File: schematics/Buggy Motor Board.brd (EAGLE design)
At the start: 100 x 80 mm, 42 parts, among them CON0 M025MM, CON1 M025MM, X1 MICROSD, X2 5566-24, X3 5566-24

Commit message: Tweak for Master
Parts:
- moved IC1 51.9 mm to (36.8, 25.4)
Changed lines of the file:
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@@
 <element name="U$10" library="Teensy_3_Series_Board_v1.0" package="TEENSY_3.1+4" value="TEENSY_3.1+4" x="36.83" y="60.96"/>
 <element name="U$1" library="Wetmelon-Connectors" package="WM9300" value="WM9300" x="5.08" y="63.5" rot="R90"/>
-<element name="IC1" library="SparkFun-PowerIC" package="78XXL" value="" x="-11.43" y="6.35"/>
+<element name="IC1" library="SparkFun-PowerIC" package="78XXL" value="" x="36.83" y="25.4"/>
 <element name="C1" library="rcl" package="C0805" value=".33uF" x="-13.97" y="-3.81"/>
 <element name="C6" library="rcl" package="C0805" value=".1uF" x="-13.97" y="-8.89"/>
@@
 <wire x1="32.8422" y1="3.81" x2="29.21" y2="8.66" width="0" layer="19" extent="1-1"/>
 <wire x1="44.2722" y1="3.81" x2="32.8422" y2="3.81" width="0" layer="19" extent="1-1"/>
-<wire x1="-11.43" y1="2.54" x2="2.07" y2="29.58" width="0" layer="19" extent="1-1"/>
-<wire x1="-13.02" y1="-3.81" x2="-11.43" y2="2.54" width="0" layer="19" extent="1-1"/>
+<wire x1="36.83" y1="21.59" x2="2.07" y2="29.58" width="0" layer="19" extent="1-1"/>
+<wire x1="-13.02" y1="-3.81" x2="36.83" y2="21.59" width="0" layer="19" extent="1-1"/>
 <wire x1="-13.02" y1="-8.89" x2="-13.02" y2="-3.81" width="0" layer="19" extent="1-1"/>
 </signal>
@@
 <wire x1="29.21" y1="11.66" x2="50.8" y2="31.75" width="0" layer="19" extent="1-1"/>
 <wire x1="24.2062" y1="17.145" x2="29.21" y2="11.66" width="0" layer="19" extent="1-1"/>
-<wire x1="-8.89" y1="2.54" x2="24.2062" y2="17.145" width="0" layer="19" extent="1-1"/>
-<wire x1="-14.92" y1="-8.89" x2="-8.89" y2="2.54" width="0" layer="19" extent="1-1"/>
+<wire x1="39.37" y1="21.59" x2="24.2062" y2="17.145" width="0" layer="19" extent="1-1"/>
+<wire x1="-14.92" y1="-8.89" x2="39.37" y2="21.59" width="0" layer="19" extent="1-1"/>
 </signal>
 <signal name="MISO">
@@
 <wire x1="49.9" y1="54.61" x2="49.9" y2="57.15" width="0" layer="19" extent="1-1"/>
 <wire x1="49.9" y1="52.07" x2="49.9" y2="54.61" width="0" layer="19" extent="1-1"/>
-<wire x1="-13.97" y1="2.54" x2="49.9" y2="52.07" width="0" layer="19" extent="1-1"/>
-<wire x1="-14.92" y1="-3.81" x2="-13.97" y2="2.54" width="0" layer="19" extent="1-1"/>
+<wire x1="34.29" y1="21.59" x2="49.9" y2="52.07" width="0" layer="19" extent="1-1"/>
+<wire x1="-14.92" y1="-3.81" x2="34.29" y2="21.59" width="0" layer="19" extent="1-1"/>
 </signal>
 <signal name="CHAN0">

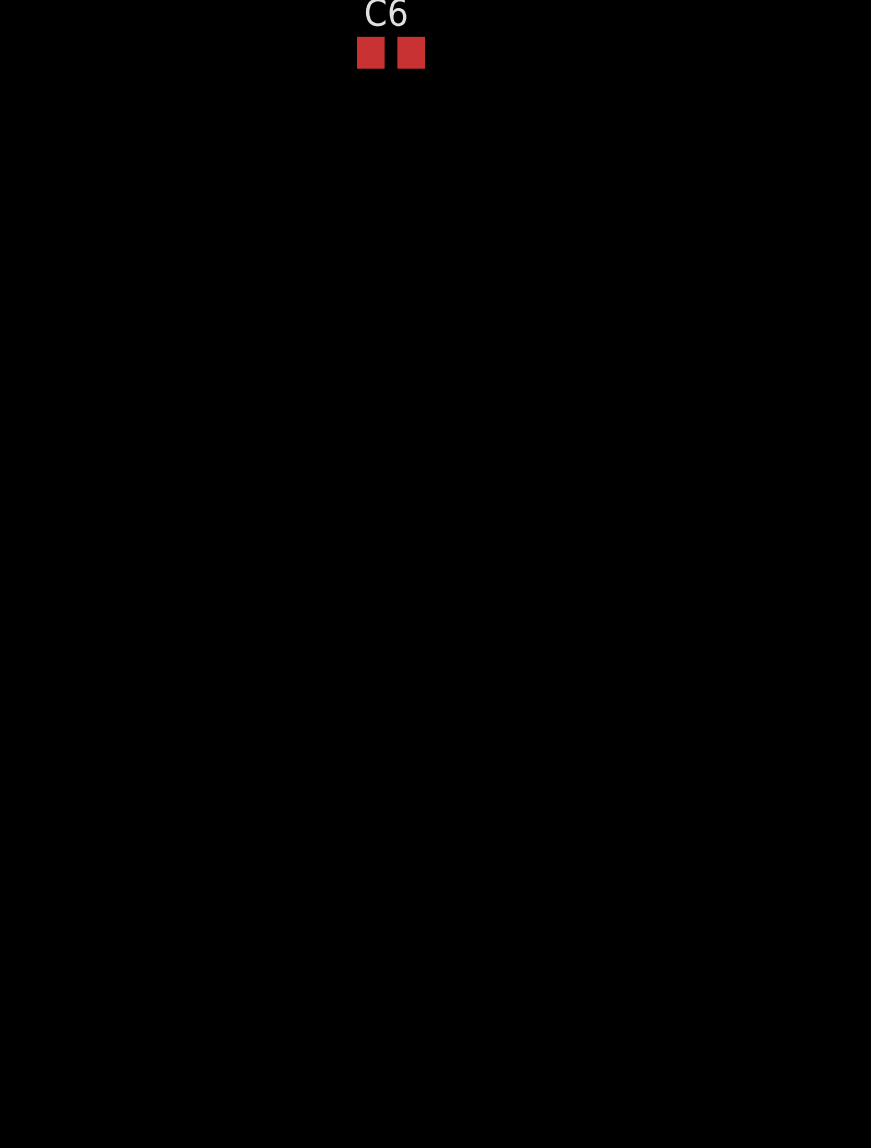
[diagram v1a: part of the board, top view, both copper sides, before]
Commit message: Add Quadrature Counter, RTC, MPU, CAN Bus 2
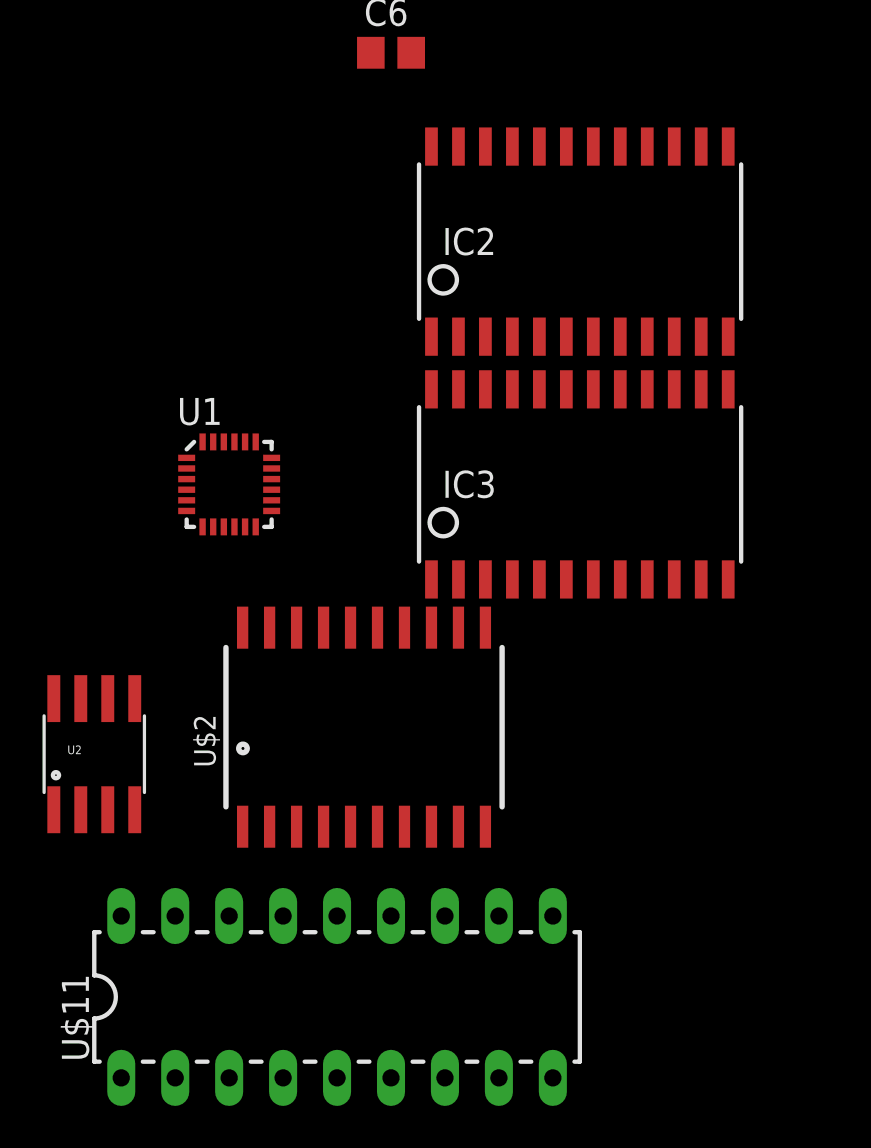
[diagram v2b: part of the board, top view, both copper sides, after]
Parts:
- added IC2, IC3: LS7766SO-S, lsi-computer-systems:SOIC24L
- added U$11: MCP2515, Wetmelon-DigitalIC:DIL18
- added U$2: DS3234, SparkFun-FreqCtrl:DS3234
- added U1: (no value), SparkFun-Sensors:QFN-24-NP
- added U2: MCP2562, Wetmelon-DigitalIC:SO08
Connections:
- net +3V3: now also IC2.24, IC3.24
- net GND: now also IC2.12, IC3.12
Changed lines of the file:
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@@
 <element name="C1" library="rcl" package="C0805" value=".33uF" x="-13.97" y="-3.81"/>
 <element name="C6" library="rcl" package="C0805" value=".1uF" x="-13.97" y="-8.89"/>
+<element name="IC2" library="lsi-computer-systems" package="SOIC24L" value="LS7766SO-S" x="-5.08" y="-17.78"/>
+<element name="IC3" library="lsi-computer-systems" package="SOIC24L" value="LS7766SO-S" x="-5.08" y="-29.21"/>
+<element name="U1" library="SparkFun-Sensors" package="QFN-24-NP" value="" x="-21.59" y="-29.21"/>
+<element name="U$2" library="SparkFun-FreqCtrl" package="DS3234" value="DS3234" x="-15.24" y="-40.64"/>
+<element name="U2" library="Wetmelon-DigitalIC" package="SO08" value="MCP2562" x="-27.94" y="-41.91"/>
+<element name="U$11" library="Wetmelon-DigitalIC" package="DIL18" value="MCP2515" x="-16.51" y="-53.34"/>
 </elements>
 <signals>
@@
 <contactref element="U$10" pad="GND1"/>
 <contactref element="U$10" pad="GND"/>
+<contactref element="IC2" pad="12"/>
+<contactref element="IC3" pad="12"/>
 <wire x1="29.21" y1="78.74" x2="52.2478" y2="76.2" width="0" layer="19" extent="1-1"/>
 <wire x1="25.03" y1="60.96" x2="29.21" y2="78.74" width="0" layer="19" extent="1-1"/>
@@
 <wire x1="53.2638" y1="38.735" x2="36.83" y2="45.72" width="0" layer="19" extent="1-1"/>
 <wire x1="53.34" y1="31.75" x2="53.2638" y2="38.735" width="0" layer="19" extent="1-1"/>
-<wire x1="2.97" y1="42.78" x2="12.854" y2="59.925" width="0" layer="19" extent="1-1"/>
-<wire x1="5.47" y1="39.68" x2="2.97" y2="42.78" width="0" layer="19" extent="1-1"/>
-<wire x1="2.07" y1="29.58" x2="5.47" y2="39.68" width="0" layer="19" extent="1-1"/>
-<wire x1="15.24" y1="17.145" x2="2.07" y2="29.58" width="0" layer="19" extent="1-1"/>
-<wire x1="18.9738" y1="14.605" x2="15.24" y2="17.145" width="0" layer="19" extent="1-1"/>
-<wire x1="24.2062" y1="15.875" x2="18.9738" y2="14.605" width="0" layer="19" extent="1-1"/>
+<wire x1="36.83" y1="21.59" x2="53.34" y2="31.75" width="0" layer="19" extent="1-1"/>
+<wire x1="24.2062" y1="15.875" x2="36.83" y2="21.59" width="0" layer="19" extent="1-1"/>
+<wire x1="18.9738" y1="14.605" x2="24.2062" y2="15.875" width="0" layer="19" extent="1-1"/>
+<wire x1="15.24" y1="17.145" x2="18.9738" y2="14.605" width="0" layer="19" extent="1-1"/>
 <wire x1="29.21" y1="8.66" x2="24.2062" y2="15.875" width="0" layer="19" extent="1-1"/>
 <wire x1="32.8422" y1="3.81" x2="29.21" y2="8.66" width="0" layer="19" extent="1-1"/>
 <wire x1="44.2722" y1="3.81" x2="32.8422" y2="3.81" width="0" layer="19" extent="1-1"/>
-<wire x1="36.83" y1="21.59" x2="2.07" y2="29.58" width="0" layer="19" extent="1-1"/>
-<wire x1="-13.02" y1="-3.81" x2="36.83" y2="21.59" width="0" layer="19" extent="1-1"/>
+<wire x1="2.07" y1="29.58" x2="15.24" y2="17.145" width="0" layer="19" extent="1-1"/>
+<wire x1="5.47" y1="39.68" x2="2.07" y2="29.58" width="0" layer="19" extent="1-1"/>
+<wire x1="2.97" y1="42.78" x2="5.47" y2="39.68" width="0" layer="19" extent="1-1"/>
+<wire x1="-13.02" y1="-3.81" x2="15.24" y2="17.145" width="0" layer="19" extent="1-1"/>
 <wire x1="-13.02" y1="-8.89" x2="-13.02" y2="-3.81" width="0" layer="19" extent="1-1"/>
+<wire x1="1.905" y1="-22.255" x2="-13.02" y2="-8.89" width="0" layer="19" extent="1-1"/>
+<wire x1="1.905" y1="-33.685" x2="1.905" y2="-22.255" width="0" layer="19" extent="1-1"/>
 </signal>
 <signal name="MODE1">
@@
 <contactref element="U$10" pad="AREF"/>
 <contactref element="MCP-2562" pad="5"/>
+<contactref element="IC2" pad="24"/>
+<contactref element="IC3" pad="24"/>
 <wire x1="41.91" y1="71.12" x2="44.45" y2="73.66" width="0" layer="19" extent="1-1"/>
 <wire x1="34.29" y1="45.72" x2="41.91" y2="71.12" width="0" layer="19" extent="1-1"/>
@@
 <wire x1="5.47" y1="37.48" x2="34.29" y2="45.72" width="0" layer="19" extent="1-1"/>
 <wire x1="18.9738" y1="18.415" x2="5.47" y2="37.48" width="0" layer="19" extent="1-1"/>
+<wire x1="-12.065" y1="-13.305" x2="18.9738" y2="18.415" width="0" layer="19" extent="1-1"/>
+<wire x1="-12.065" y1="-24.735" x2="-12.065" y2="-13.305" width="0" layer="19" extent="1-1"/>
 </signal>
 <signal name="CD">

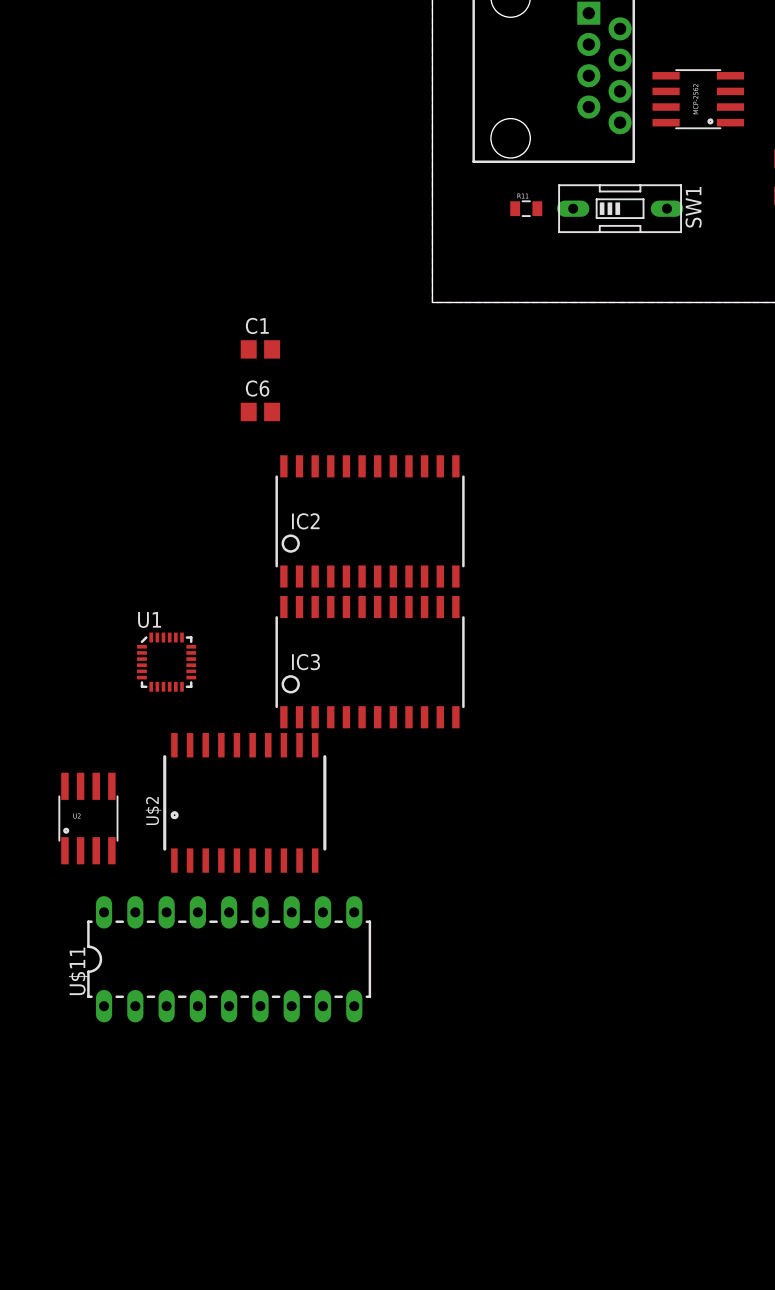
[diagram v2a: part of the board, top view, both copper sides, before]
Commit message: Schematic changes
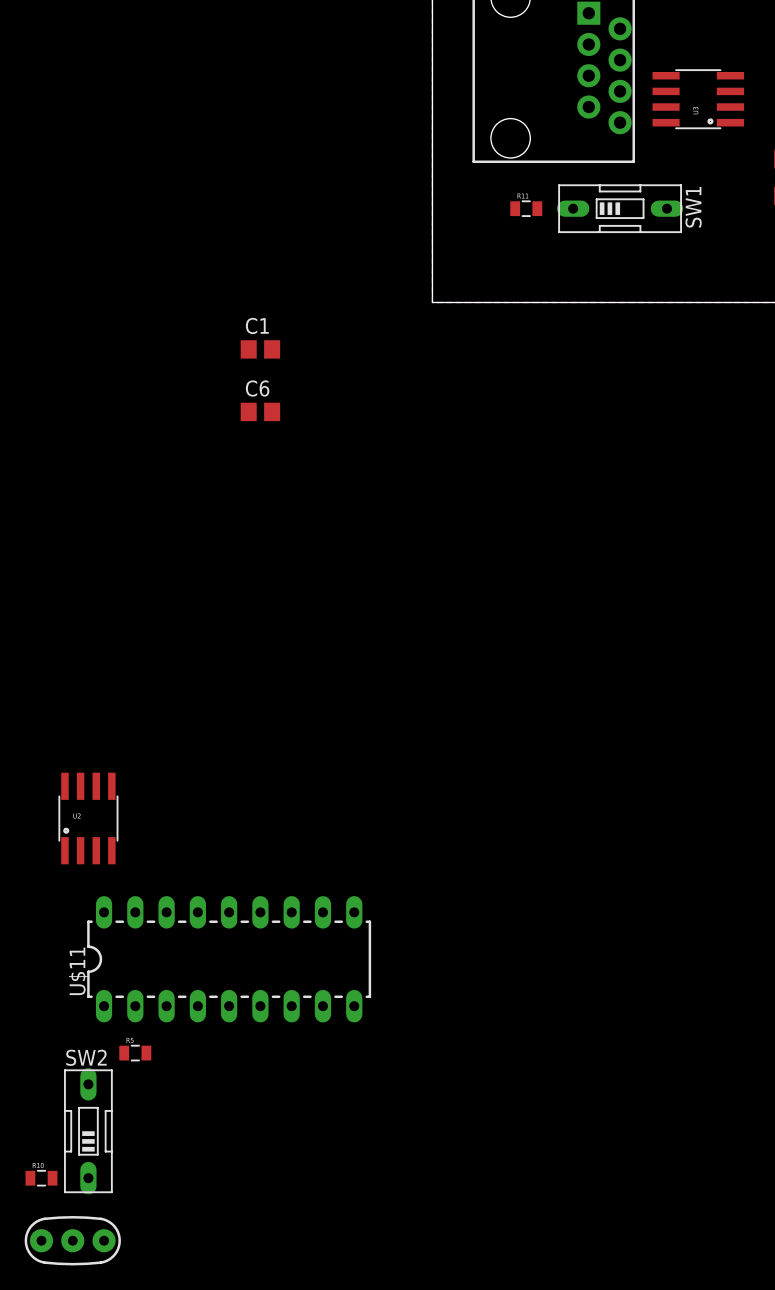
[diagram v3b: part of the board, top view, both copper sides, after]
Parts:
- removed IC2, IC3: LS7766SO-S, lsi-computer-systems:SOIC24L
- removed U$2: DS3234, SparkFun-FreqCtrl:DS3234
- removed U1: (no value), SparkFun-Sensors:QFN-24-NP
- added R10: 10k, SparkFun-Resistors:0805
- added R5: 120, SparkFun-Resistors:0805
- added SW2: (no value), special:EDG-01
- added Y1: 16MHz, SparkFun-FreqCtrl:RESONATOR-PTH
- renumbered MCP-2562 to U3
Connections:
- net CANH renamed CANH_HS
- net CANL renamed CANL_HS
- net ENC_0_A renamed ENC0_A
- net ENC_0_B renamed ENC0_B
- net ENC_0_Z renamed ENC0_Z
- net ENC_1_A renamed ENC1_A
- net ENC_1_B renamed ENC1_B
- net ENC_1_Z renamed ENC1_Z
- net RXCAN renamed RXCAN_HS
- net TXCAN renamed TXCAN_HS
- new net CANH_LS: SW2.2, U$5.5, U2.7
- new net CANL_LS: R5.1, U$5.4, U2.6
- new net CAN_INT: U$10.1, U$11.16
- new net CS_CAN: U$10.2, U$11.12
- new net LDAC: U$10.0
- new net N$1: R5.2, SW2.1
- new net N$10: U$11.8, Y1.3
- new net N$14: R10.2, U$11.11
- new net N$9: U$11.7, Y1.1
- new net RXCAN_LS: U$11.2, U2.4
- new net TXCAN_LS: U$11.1, U2.1
- net +3V3: now also R10.1, U$11.10, U2.5; no longer IC2.24, IC3.24
- net +5V: now also U2.3
- net CD: now also U$10.23/A9
- net GND: now also U$11.9, U$5.1, U$5.2, U$5.3, U2.2, U2.8, Y1.2; no longer IC2.12, IC3.12
- net MISO: now also U$11.13
- net MOSI: now also U$11.14
- net SCK: now also U$11.15
